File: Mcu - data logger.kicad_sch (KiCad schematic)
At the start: 0 parts

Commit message: new Sheet added
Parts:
- added BT1: Battery, Package_TO_SOT_SMD:SOT-23-5, symbol Device:Battery
- added C1, C2, C3, C4: C, symbol Device:C
- added C5: C_Polarized, symbol Device:C_Polarized
- added D1, D2: LED, LED_SMD:LED_Cree-XHP50_3V_HighDensity, symbol Device:LED
- added H1, H2, H3, H4: MountingHole, Module:Maple_Mini, symbol Mechanical:MountingHole
- added R1, R2, R3, R4, R5, R6, R7: R, symbol Device:R
- added U1, U2: 24LC1025, Package_SO:SOIC-8_3.9x4.9mm_P1.27mm, symbol Memory_EEPROM:24LC1025
- added U3: DS1337, DS1337:DIL08-ROUND, symbol DS1337:DS1337
- added U4: ATMEGA328P-AU, ATMEGA328P-AU:QFP80P900X900X120-32N, symbol ATMEGA328-AU:ATMEGA328P-AU
- added Y1, Y2: Crystal, symbol Device:Crystal
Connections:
- new net GND: U4.21 (GND), U4.3 (GND), U4.5 (GND)
- new net VCC: U4.4 (VCC), U4.6 (VCC)
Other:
- title: (none) -> ${project_name }

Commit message: symbols added
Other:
- added sheet Connectors (Connectors.kicad_sch)
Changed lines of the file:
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@@
+		)
+	)
+	(sheet
+		(at 119.38 148.59)
+		(size 41.91 30.48)
+		(exclude_from_sim no)
+		(in_bom yes)
+		(on_board yes)
+		(dnp no)
+		(fields_autoplaced yes)
+		(stroke
+			(width 0.1524)
+			(type solid)
+		)
+		(fill
+			(color 0 0 0 0)
+		)
+		(property "Sheetname" "Connectors"
+			(at 119.38 147.8784 0)
+			(show_name no)
+			(do_not_autoplace no)
+			(effects
+				(font
+					(size 1.27 1.27)
+				)
+				(justify left bottom)
+			)
+		)
+		(property "Sheetfile" "Connectors.kicad_sch"
+			(at 119.38 179.6546 0)
+			(show_name no)
+			(do_not_autoplace no)
+			(effects
+				(font
+					(size 1.27 1.27)
+				)
+				(justify left top)
+			)
+		)
+		(instances
+			(project "Mcu - data logger"
+				(path "/33dac713-6b0b-4078-a50e-6224d6a6b582"
+					(page "2")
+				)
+			)
 		)
 	)

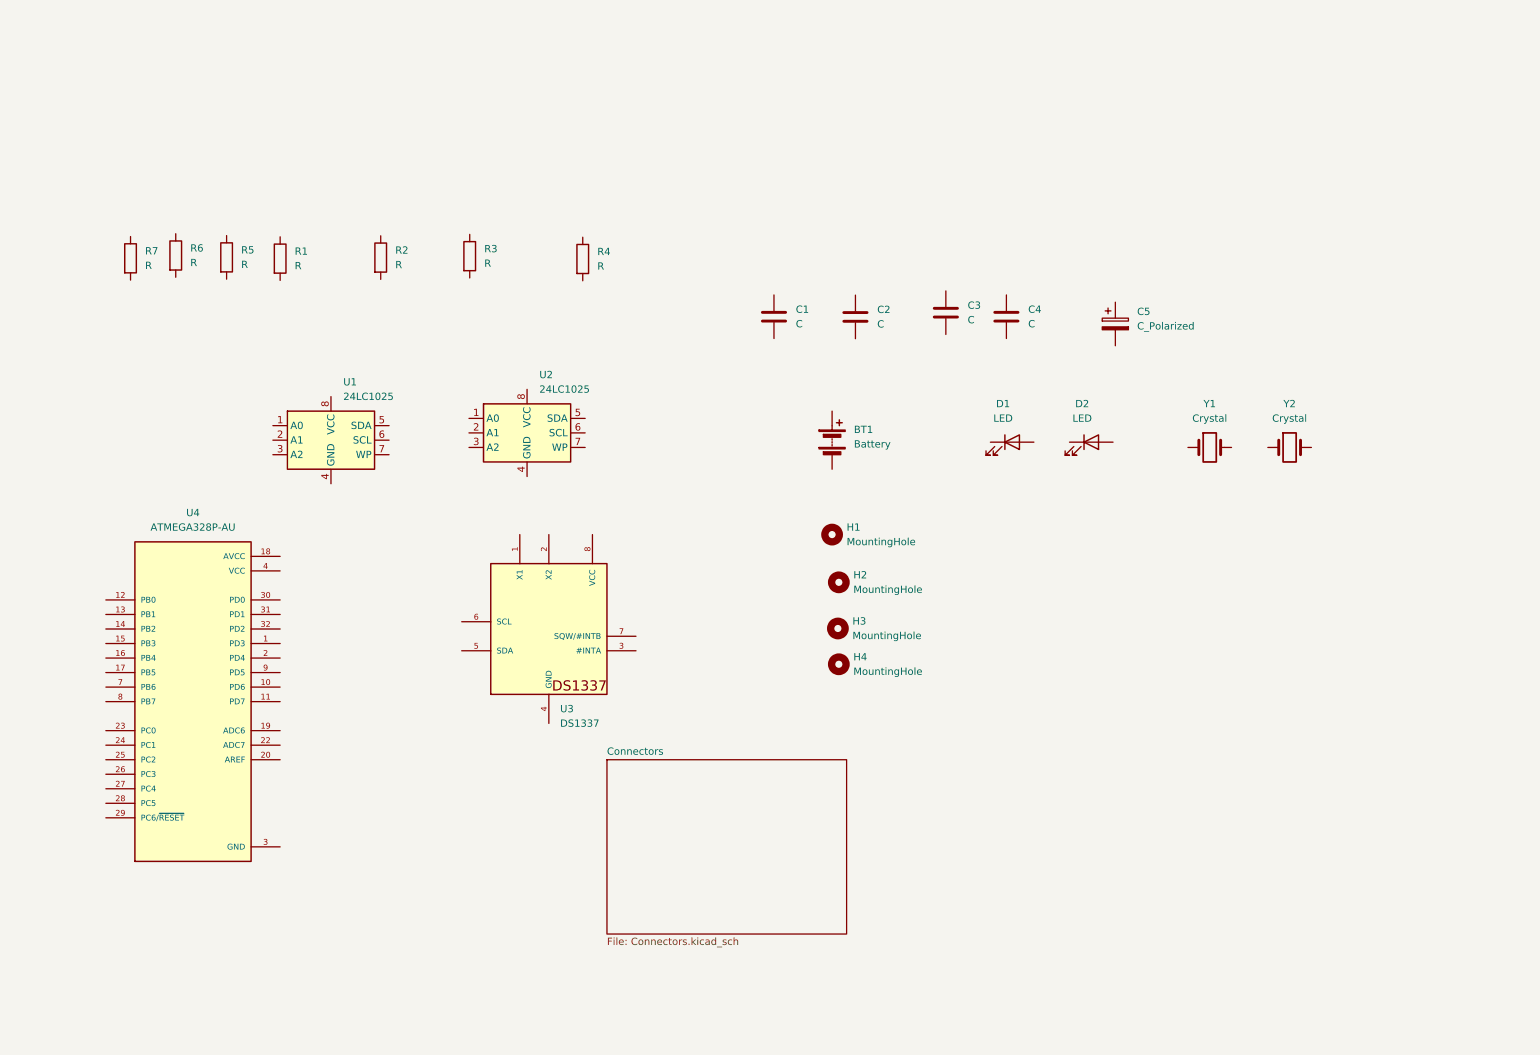
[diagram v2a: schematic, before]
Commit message: components value added
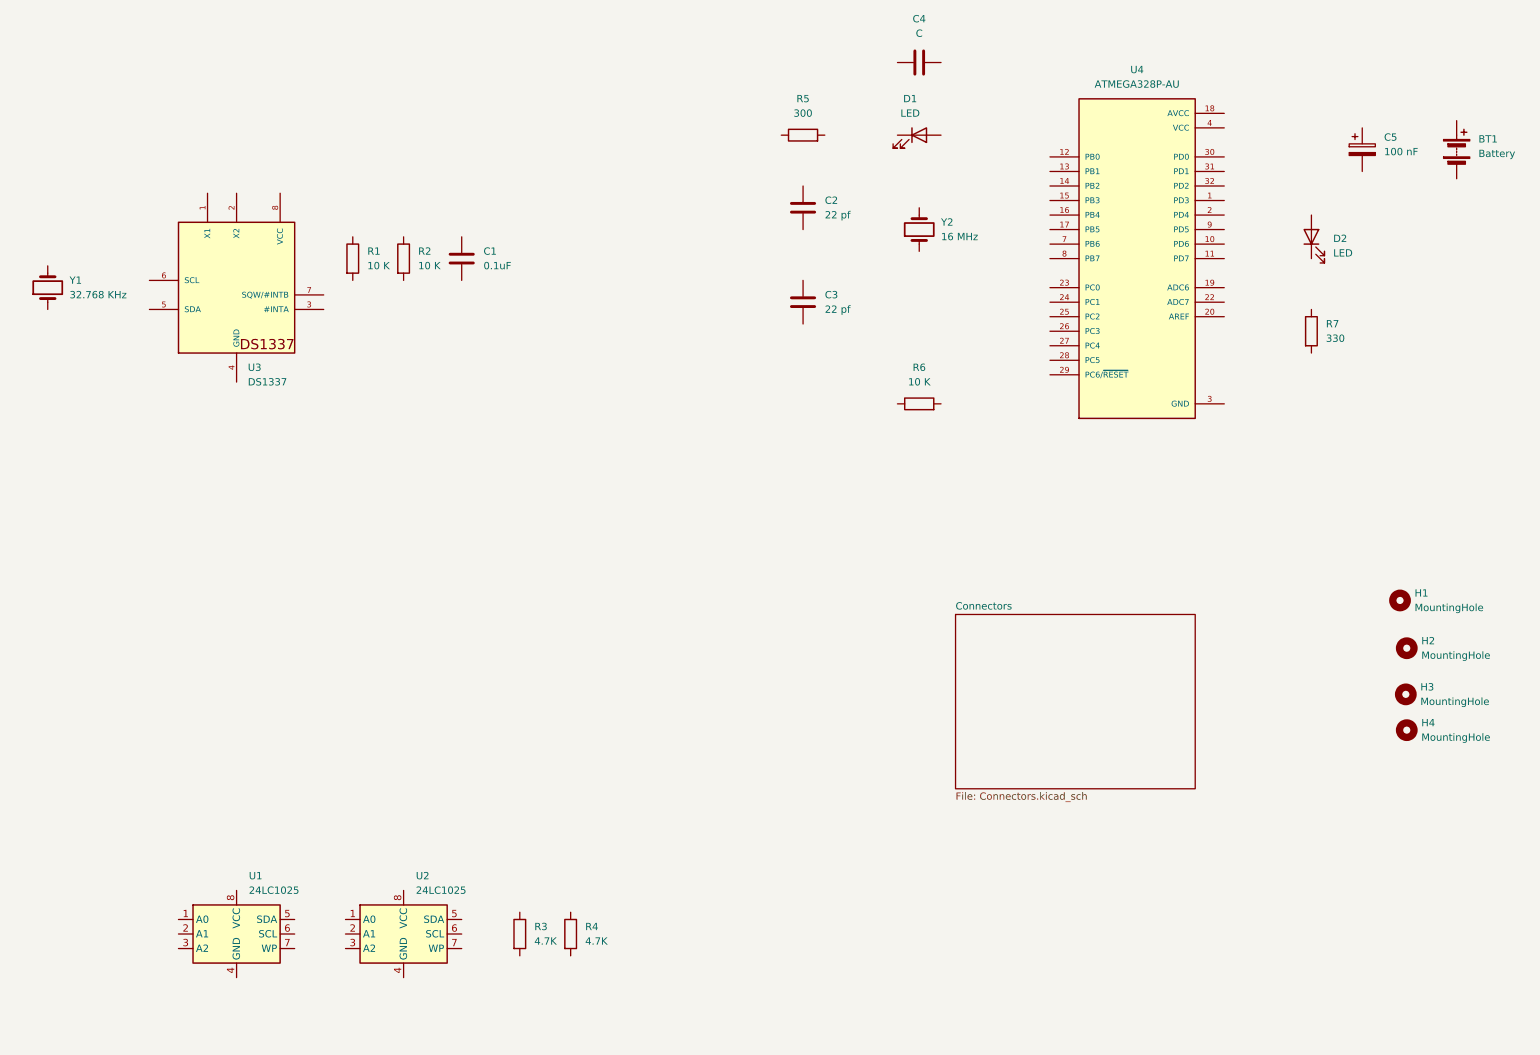
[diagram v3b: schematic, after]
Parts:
- C1: renamed from C4; value C -> 0.1uF
- C2, C3: value C -> 22 pf
- C5: value C_Polarized -> 100 nF
- R1: renamed from R7; value R -> 10 K
- R2: renamed from R6; value R -> 10 K
- R3: renamed from R5; value R -> 4.7K
- R4: renamed from R1; value R -> 4.7K
- R5: renamed from R3; value R -> 300
- R6: renamed from R2; value R -> 10 K
- R7: renamed from R4; value R -> 330
- Y1: renamed from Y2; value Crystal -> 32.768 KHz
- Y2: renamed from Y1; value Crystal -> 16 MHz
- renumbered C1 to C4, D2 to D1, D1 to D2
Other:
- moved on the sheet: BT1, C1, C2, C3, C4, C5, D1, D2, H1, H2, H3, H4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

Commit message: Wiring sheet 1
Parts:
- C1, C2, C3, C4, C5: footprint (none) -> Capacitor_SMD:C_0805_2012Metric
- D1, D2: footprint LED_SMD:LED_Cree-XHP50_3V_HighDensity -> LED_SMD:LED_0805_2012Metric
- H1, H2, H3, H4: footprint Module:Maple_Mini -> MountingHole:MountingHole_2.1mm
- R1, R2, R3, R4, R5, R6, R7: footprint (none) -> Resistor_SMD:R_0805_2012Metric
- U1: footprint Package_SO:SOIC-8_3.9x4.9mm_P1.27mm -> Package_SO:SOIC-8_5.3x6.2mm_P1.27mm
- Y1, Y2: footprint (none) -> Crystal:Crystal_SMD_5032-2Pin_5.0x3.2mm_HandSoldering
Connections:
- net GND: now also BT1.2 (-), C1.2, C2.1, C3.1, C4.1, C5.2, R5.1, R7.2, U1.4 (GND), U1.7 (WP), U2.3 (A2), U2.4 (GND), U3.4 (GND)
- net at R1.1: now also C1.1, R2.1, U3.8 (VCC)
- net at R1.2: now also U3.3 (#INTA)
- net D8: now reaches C4.2
- net D8: now also U4.12 (PB0)
- net at BT1.1 (+): now also C5.1, D2.2 (A), U4.18 (AVCC), U4.4 (VCC)
- net D3: now reaches U4.1 (PD3)
- net D6: now reaches U4.10 (PD6)
- net D7: now reaches U4.11 (PD7)
- net SCK: now reaches U4.17 (PB5)
- net SCK: now also D1.2 (A), U1.6 (SCL)
- net D4: now reaches U4.2 (PD4)
- net RESET: now reaches U4.29 (PC6/~{RESET})
- net RESET: now also R6.2
- net TX: now reaches U4.30 (PD0)
- net RX: now reaches U4.31 (PD1)
- net D2: now reaches U4.32 (PD2)
- net at U4.7 (PB6): now also C2.2, Y2.2
- net at U4.8 (PB7): now also C3.2, Y2.1
- net D5: now reaches U4.9 (PD5)
- net at R5.2: now also D1.1 (K)
- net at U3.1 (X1): now also Y1.2
- net at U3.2 (X2): now also Y1.1
- net at U3.7 (SQW/#INTB): now also R2.2
- net at R3.1: now also R4.1
- net SDA: now reaches U1.5 (SDA)
- net at R7.1: now also D2.1 (K)
- net VCC: no longer names the net of U4.6 (VCC)
- net VCC: no longer U4.4 (VCC)
- no-connect marks 0 -> 9
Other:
- moved on the sheet: BT1, C2, C3, C5, D2, R6, Y2
